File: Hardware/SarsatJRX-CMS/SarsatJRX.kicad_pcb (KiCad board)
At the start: 2 copper layers, 65 x 56.5 mm, 58 parts, among them J3 LilyPi GPIO Header, Q1 S8050, U1 TLC2274, U2 TLC2274

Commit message: Fixed some silkscreen
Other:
- board text added: "F4JRX ADRASEC 31"
- board text added: "SarsatJRX v1.1 08/2025"
- board text removed: "SarsatJRX v1.1 - 08/2025 F4JRX - ADRASEC 31"
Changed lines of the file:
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@@
 		(tags "test point SMD pad")
 		(property "Reference" "TP5"
-			(at 2.423503 0.053473 0)
+			(at 0.010503 1.831473 0)
 			(layer "F.SilkS")
 			(effects
@@
 		(tags "resistor")
 		(property "Reference" "R3"
-			(at 0 1.524 90)
+			(at 0.127 -1.524 90)
 			(layer "F.SilkS")
 			(effects
@@
 		(tags "test point SMD pad")
 		(property "Reference" "TP6"
-			(at 0 -1.448 0)
+			(at 0 -1.524 0)
 			(layer "F.SilkS")
 			(effects
@@
 	)
 	(gr_text "Frame"
-		(at 166.729 105.775 0)
+		(at 165.84 106.029 0)
 		(layer "F.SilkS")
 		(effects
 			(font
-				(size 1 1)
-				(thickness 0.15)
+				(size 1.5 1.5)
+				(thickness 0.3)
+				(bold yes)
 			)
 			(justify left bottom)
 		)
 	)
+	(gr_text "F4JRX\nADRASEC 31"
+		(at 168.761 99.679 0)
+		(layer "F.SilkS")
+		(effects
+			(font
+				(size 1.5 1.5)
+				(thickness 0.3)
+				(bold yes)
+			)
+			(justify bottom)
+		)
+	)
 	(gr_text "5V"
 		(at 117.199 64.5 0)
@@
 	)
 	(gr_text "Deriv. adj."
-		(at 121.517 69.199 0)
+		(at 121.136 69.326 0)
 		(layer "F.SilkS")
 		(effects
 			(font
-				(size 1 1)
-				(thickness 0.15)
+				(size 1.1 1.1)
+				(thickness 0.275)
+				(bold yes)
 			)
 			(justify left bottom)
@@
 	)
 	(gr_text "Error\n"
-		(at 160.125 105.775 0)
+		(at 159.109 106.029 0)
 		(layer "F.SilkS")
 		(effects
 			(font
-				(size 1 1)
-				(thickness 0.15)
+				(size 1.5 1.5)
+				(thickness 0.3)
+				(bold yes)
 			)
 			(justify left bottom)
@@
 		)
 	)
-	(gr_text "SarsatJRX v1.1 - 08/2025\nF4JRX - ADRASEC 31"
-		(at 147.679 78.343 0)
+	(gr_text "SarsatJRX v1.1\n08/2025"
+		(at 147.552 78.978 0)
 		(layer "F.SilkS")
 		(effects
 			(font
-				(size 1 1)
-				(thickness 0.15)
+				(size 1.5 1.5)
+				(thickness 0.3)
+				(bold yes)
 			)
 			(justify bottom)
@@
 	)
 	(gr_text "Deco. adj."
-		(at 160.887 69.326 0)
+		(at 160.506 69.453 0)
 		(layer "F.SilkS")
 		(effects
 			(font
-				(size 1 1)
-				(thickness 0.15)
+				(size 1.1 1.1)
+				(thickness 0.275)
+				(bold yes)
 			)
 			(justify left bottom)
@@
 	)
 	(gr_text "Signal"
-		(at 151.616 105.775 0)
+		(at 151.489 106.029 0)
 		(layer "F.SilkS")
 		(effects
 			(font
-				(size 1 1)
-				(thickness 0.15)
+				(size 1.5 1.5)
+				(thickness 0.3)
+				(bold yes)
 			)
 			(justify bottom)

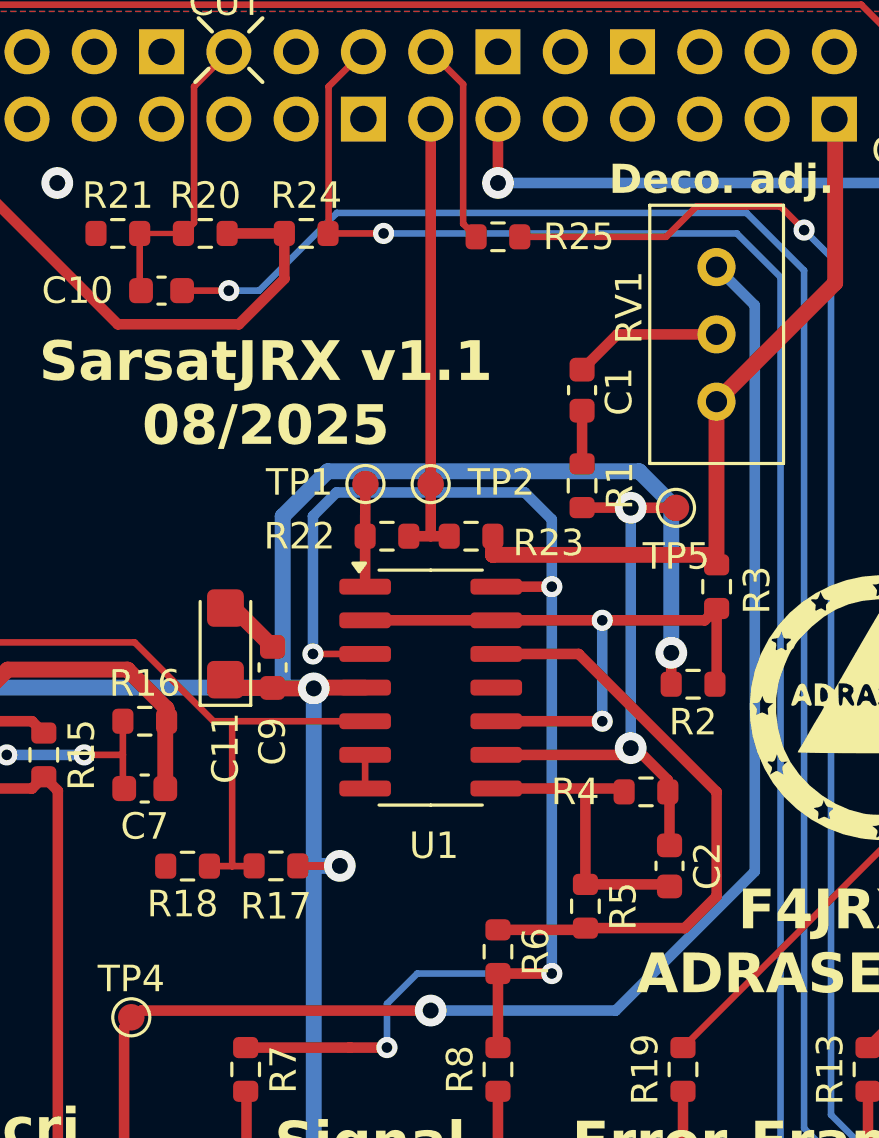
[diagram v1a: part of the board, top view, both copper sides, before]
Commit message: Fixed more silk screen. Added 2 test points.
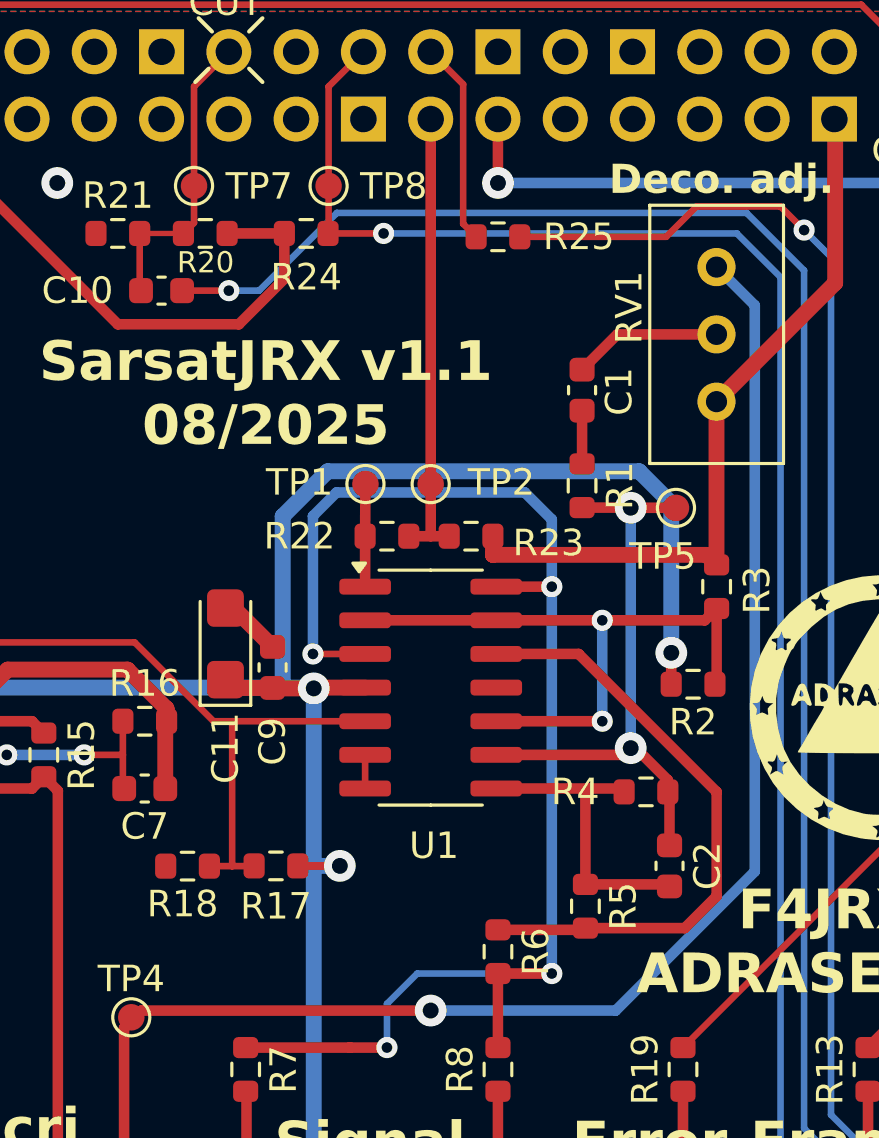
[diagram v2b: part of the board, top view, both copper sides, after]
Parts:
- added TP7: ~, TestPoint:TestPoint_Pad_D1.0mm, F.Cu at (144.8, 69.1)
- added TP8: ~, TestPoint:TestPoint_Pad_D1.0mm, F.Cu at (149.9, 69.1)
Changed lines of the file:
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@@
 		(tags "resistor")
 		(property "Reference" "R20"
-			(at 0 -1.43 0)
+			(at 0.011568 1.097628 0)
 			(layer "F.SilkS")
 			(effects
 				(font
-					(size 1 1)
-					(thickness 0.15)
+					(size 0.8 0.8)
+					(thickness 0.1)
 				)
 			)
@@
 		(tags "test point SMD pad")
 		(property "Reference" "TP5"
-			(at 0.010503 1.831473 0)
+			(at -0.497497 1.831473 0)
 			(layer "F.SilkS")
 			(effects
@@
 		(embedded_fonts no)
 	)
+	(footprint "TestPoint:TestPoint_Pad_D1.0mm"
+		(layer "F.Cu")
+		(at 144.841 69.056565)
+		(descr "SMD pad as test Point, diameter 1.0mm")
+		(tags "test point SMD pad")
+		(property "Reference" "TP7"
+			(at 2.457 0.015435 0)
+			(layer "F.SilkS")
+			(effects
+				(font
+					(size 1 1)
+					(thickness 0.15)
+				)
+			)
+		)
+		(property "Value" "~"
+			(at 0 1.55 0)
+			(layer "F.Fab")
+			(effects
+				(font
+					(size 1 1)
+					(thickness 0.15)
+				)
+			)
+		)
+		(property "Datasheet" ""
+			(at 0 0 0)
+			(unlocked yes)
+			(layer "F.Fab")
+			(hide yes)
+			(effects
+				(font
+					(size 1.27 1.27)
+					(thickness 0.15)
+				)
+			)
+		)
+		(property "Description" "test point"
+			(at 0 0 0)
+			(unlocked yes)
+			(layer "F.Fab")
+			(hide yes)
+			(effects
+				(font
+					(size 1.27 1.27)
+					(thickness 0.15)
+				)
+			)
+		)
+		(property ki_fp_filters "Pin* Test*")
+		(sheetname "/")
+		(sheetfile "SarsatJRX.kicad_sch")
+		(attr exclude_from_pos_files)
+		(fp_circle
+			(center 0 0)
+			(end 0 0.7)
+			(stroke
+				(width 0.12)
+				(type solid)
+			)
+			(fill no)
+			(layer "F.SilkS")
+		)
+		(fp_circle
+			(center 0 0)
+			(end 1 0)
+			(stroke
+				(width 0.05)
+				(type solid)
+			)
+			(fill no)
+			(layer "F.CrtYd")
+		)
+		(fp_text user "${REFERENCE}"
+			(at 0 -1.45 0)
+			(layer "F.Fab")
+			(effects
+				(font
+					(size 1 1)
+					(thickness 0.15)
+				)
+			)
+		)
+		(pad "1" smd circle
+			(at 0 0)
+			(size 1 1)
+			(layers "F.Cu" "F.Mask")
+			(net 23 "Net-(J3-IO34)")
+			(pinfunction "1")
+			(pintype "passive")
+		)
+		(embedded_fonts no)
+	)
 	(footprint "Resistor_SMD:R_0603_1608Metric"
 		(layer "F.Cu")
@@
 		(tags "resistor")
 		(property "Reference" "R24"
-			(at 0 -1.43 0)
+			(at 0 1.651 0)
 			(layer "F.SilkS")
 			(effects
@@
 		)
 	)
+	(footprint "TestPoint:TestPoint_Pad_D1.0mm"
+		(layer "F.Cu")
+		(at 149.921 69.056565)
+		(descr "SMD pad as test Point, diameter 1.0mm")
+		(tags "test point SMD pad")
+		(property "Reference" "TP8"
+			(at 2.457 0.015435 0)
+			(layer "F.SilkS")
+			(effects
+				(font
+					(size 1 1)
+					(thickness 0.15)
+				)
+			)
+		)
+		(property "Value" "~"
+			(at 0 1.55 0)
+			(layer "F.Fab")
+			(effects
+				(font
+					(size 1 1)
+					(thickness 0.15)
+				)
+			)
+		)
+		(property "Datasheet" ""
+			(at 0 0 0)
+			(unlocked yes)
+			(layer "F.Fab")
+			(hide yes)
+			(effects
+				(font
+					(size 1.27 1.27)
+					(thickness 0.15)
+				)
+			)
+		)
+		(property "Description" "test point"
+			(at 0 0 0)
+			(unlocked yes)
+			(layer "F.Fab")
+			(hide yes)
+			(effects
+				(font
+					(size 1.27 1.27)
+					(thickness 0.15)
+				)
+			)
+		)
+		(property ki_fp_filters "Pin* Test*")
+		(sheetname "/")
+		(sheetfile "SarsatJRX.kicad_sch")
+		(attr exclude_from_pos_files)
+		(fp_circle
+			(center 0 0)
+			(end 0 0.7)
+			(stroke
+				(width 0.12)
+				(type solid)
+			)
+			(fill no)
+			(layer "F.SilkS")
+		)
+		(fp_circle
+			(center 0 0)
+			(end 1 0)
+			(stroke
+				(width 0.05)
+				(type solid)
+			)
+			(fill no)
+			(layer "F.CrtYd")
+		)
+		(fp_text user "${REFERENCE}"
+			(at 0 -1.45 0)
+			(layer "F.Fab")
+			(effects
+				(font
+					(size 1 1)
+					(thickness 0.15)
+				)
+			)
+		)
+		(pad "1" smd circle
+			(at 0 0)
+			(size 1 1)
+			(layers "F.Cu" "F.Mask")
+			(net 42 "Net-(J3-IO39)")
+			(pinfunction "1")
+			(pintype "passive")
+		)
+		(embedded_fonts no)
+	)
 	(footprint "Capacitor_Tantalum_SMD:CP_EIA-3216-18_Kemet-A"
 		(layer "F.Cu")
@@
 	(segment
 		(start 158.347 98.79)
-		(end 158.347 86.725)
-		(width 0.4)
-		(layer "B.Cu")
-		(net 14)
-	)
-	(segment
-		(start 158.347 86.725)
 		(end 158.347 84.185)
 		(width 0.4)
